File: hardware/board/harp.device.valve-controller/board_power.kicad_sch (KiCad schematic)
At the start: 21 parts, among them J8 Screw_Terminal_01x02, Q2 GSFD4005, U15 LMR51430, U7 rt6150b-33gqw

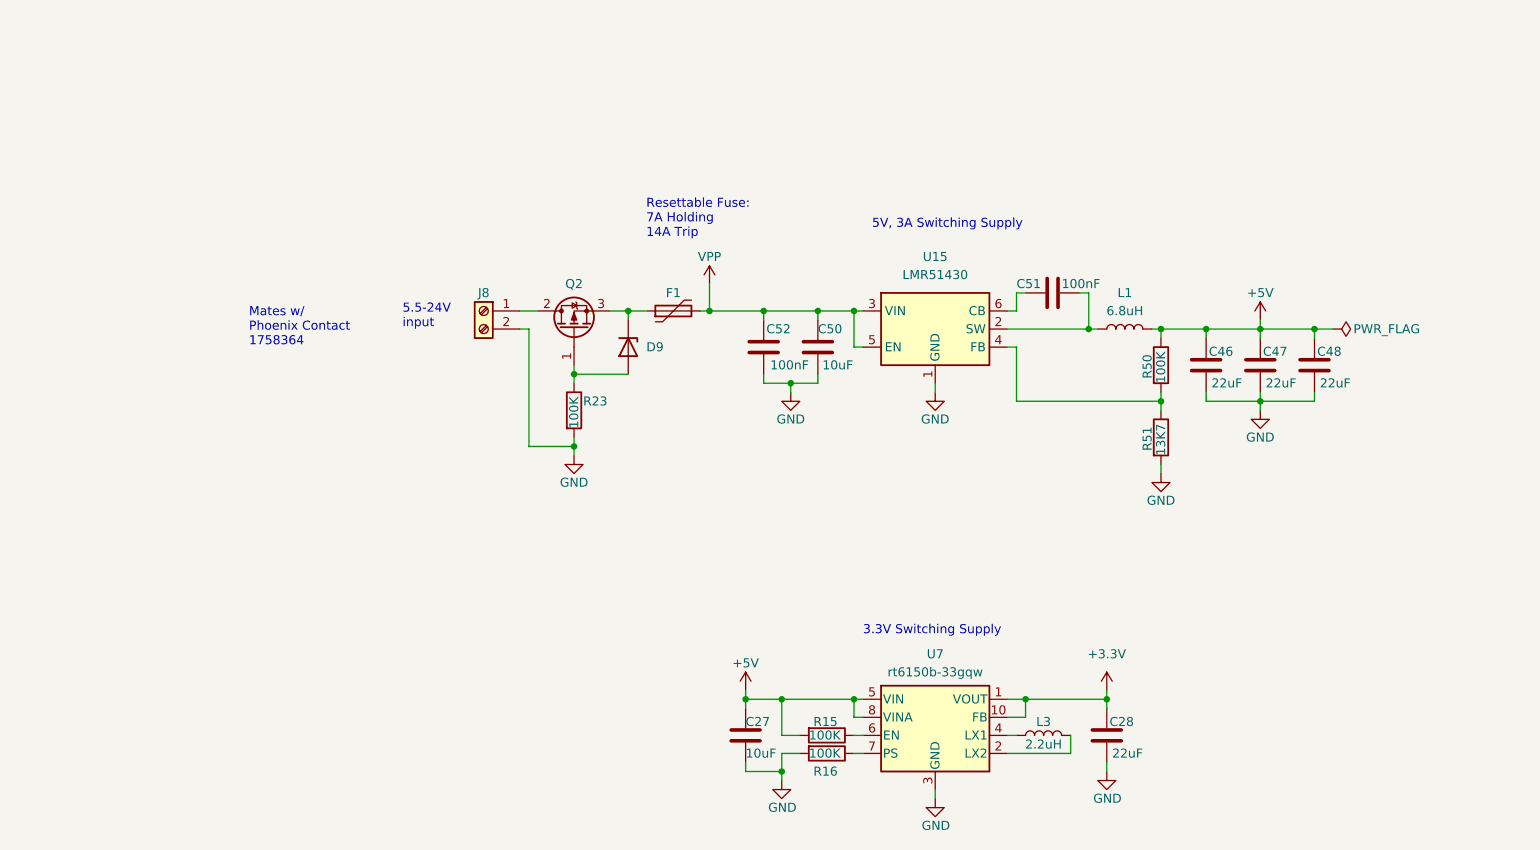
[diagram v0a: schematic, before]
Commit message: add soft start ic; add status LEDs per output
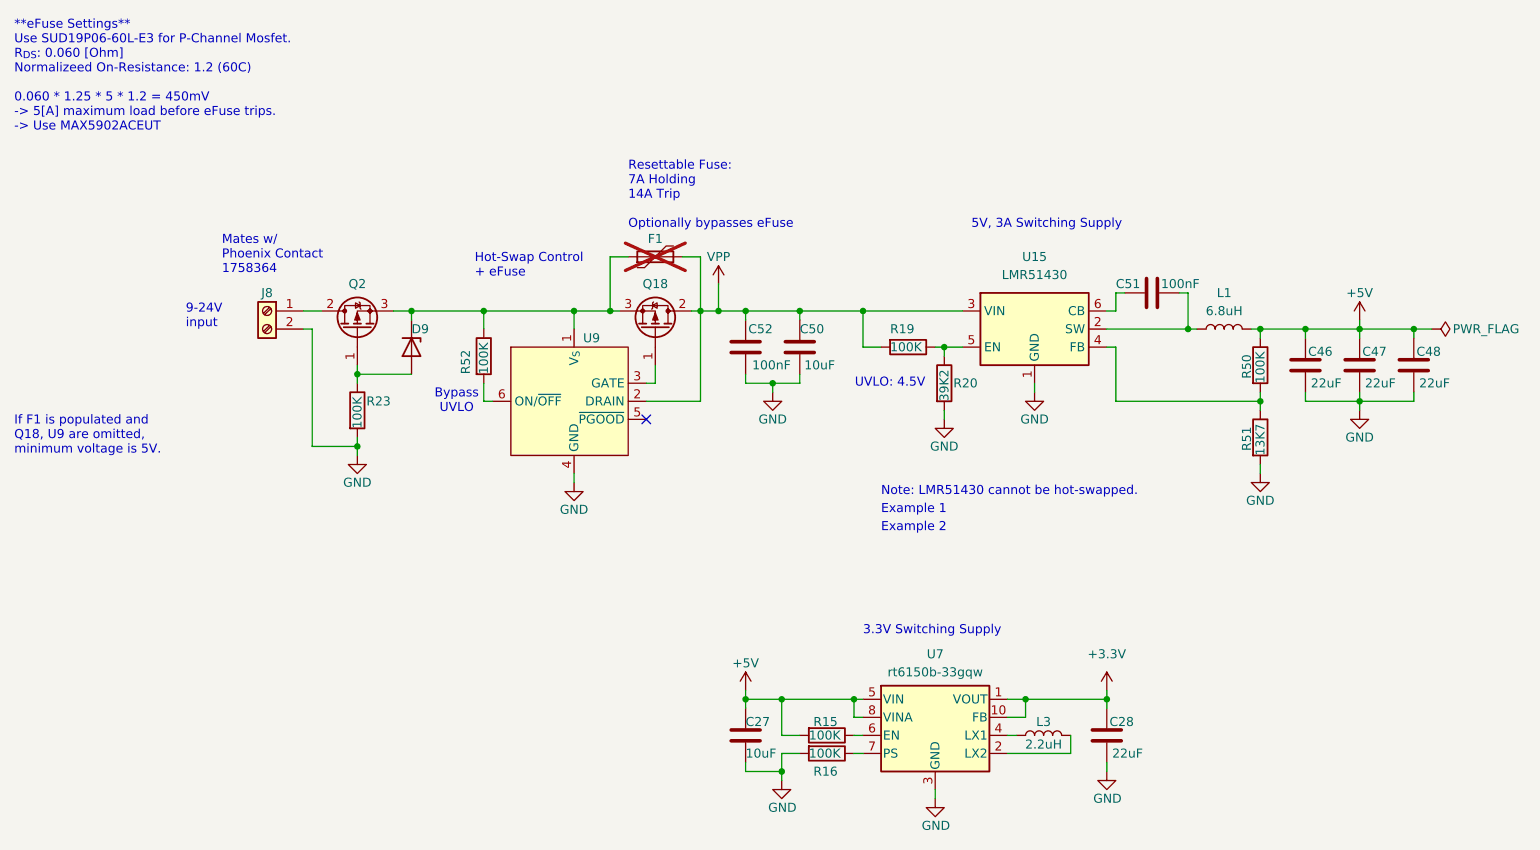
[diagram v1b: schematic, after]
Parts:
- added Q18: SUD19P06-60L-E3, Package_TO_SOT_SMD:TO-252-2, symbol Transistor_FET:SUD45P03-09
- added R19, R52: 100K, Resistor_SMD:R_0402_1005Metric, symbol Device:R
- added R20: 39K2, Resistor_SMD:R_0402_1005Metric, symbol Device:R
- added U9: ~, Package_TO_SOT_SMD:SOT-23-6, symbol kicad_component_library:MAX5902
- F1: now not fitted
- J8: Notes mates with Phoenix Contact 1758364 -> mates with Phoenix Contact 1758364 or 1757019
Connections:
- net GND: now also R20.2, U9.4 (GND)
- net VPP: now also Q18.2 (D), R19.2, U9.2 (DRAIN); no longer U15.5 (EN)
- net at D9.1 (K), F1.1, Q2.3 (S): now also Q18.3 (S), R52.1, U9.1 (V_{S})
- new net: R19.1, R20.1, U15.5 (EN)
- new net: Q18.1 (G), U9.3 (GATE)
- new net: R52.2, U9.6 (ON/~{OFF})
- no-connect marks 0 -> 1
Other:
- note added: "**eFuse Settings** Use SUD19P06-60L-E3 for P-Channel Mosfet. R_{DS}: 0.060 [Ohm] Normalizeed On-Resistance: 1.2 (60C) 0.060 * 1.25 * 5 * 1.2 = 450mV -> 5[A] maximum load before eFuse trips. -> Use MAX5902ACEUT"
- note added: "9-24V input"
- note added: "Bypass UVLO"
- note added: "Example 1"
- note added: "Example 2"
- note added: "Hot-Swap Control + eFuse"
- note added: "If F1 is populated and Q18, U9 are omitted, minimum voltage is 5V."
- note added: "Note: LMR51430 cannot be hot-swapped."
- note added: "Resettable Fuse: 7A Holding 14A Trip Optionally bypasses eFuse"
- note added: "UVLO: 4.5V"
- note removed: "5.5-24V input"
- note removed: "Resettable Fuse: 7A Holding 14A Trip"
- moved on the sheet: C46, C47, C48, C50, C51, C52, D9, J8, L1, Q2, R23, R50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
